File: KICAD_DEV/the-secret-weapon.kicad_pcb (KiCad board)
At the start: 6 copper layers, 150 x 150 mm, 44 parts, among them J1 USB_C_Receptacle_USB2.0_14P, J2 Screw_Terminal_01x02, SW1 SW_Push, SW2 SW_Push, U1 STM32H743VITx, U2 USBLC6-2SC6, U3 LMR33640ADDA, U4 LM1086S-3.3/TR, Y1 8 MHz, Y2 32.768 KHz

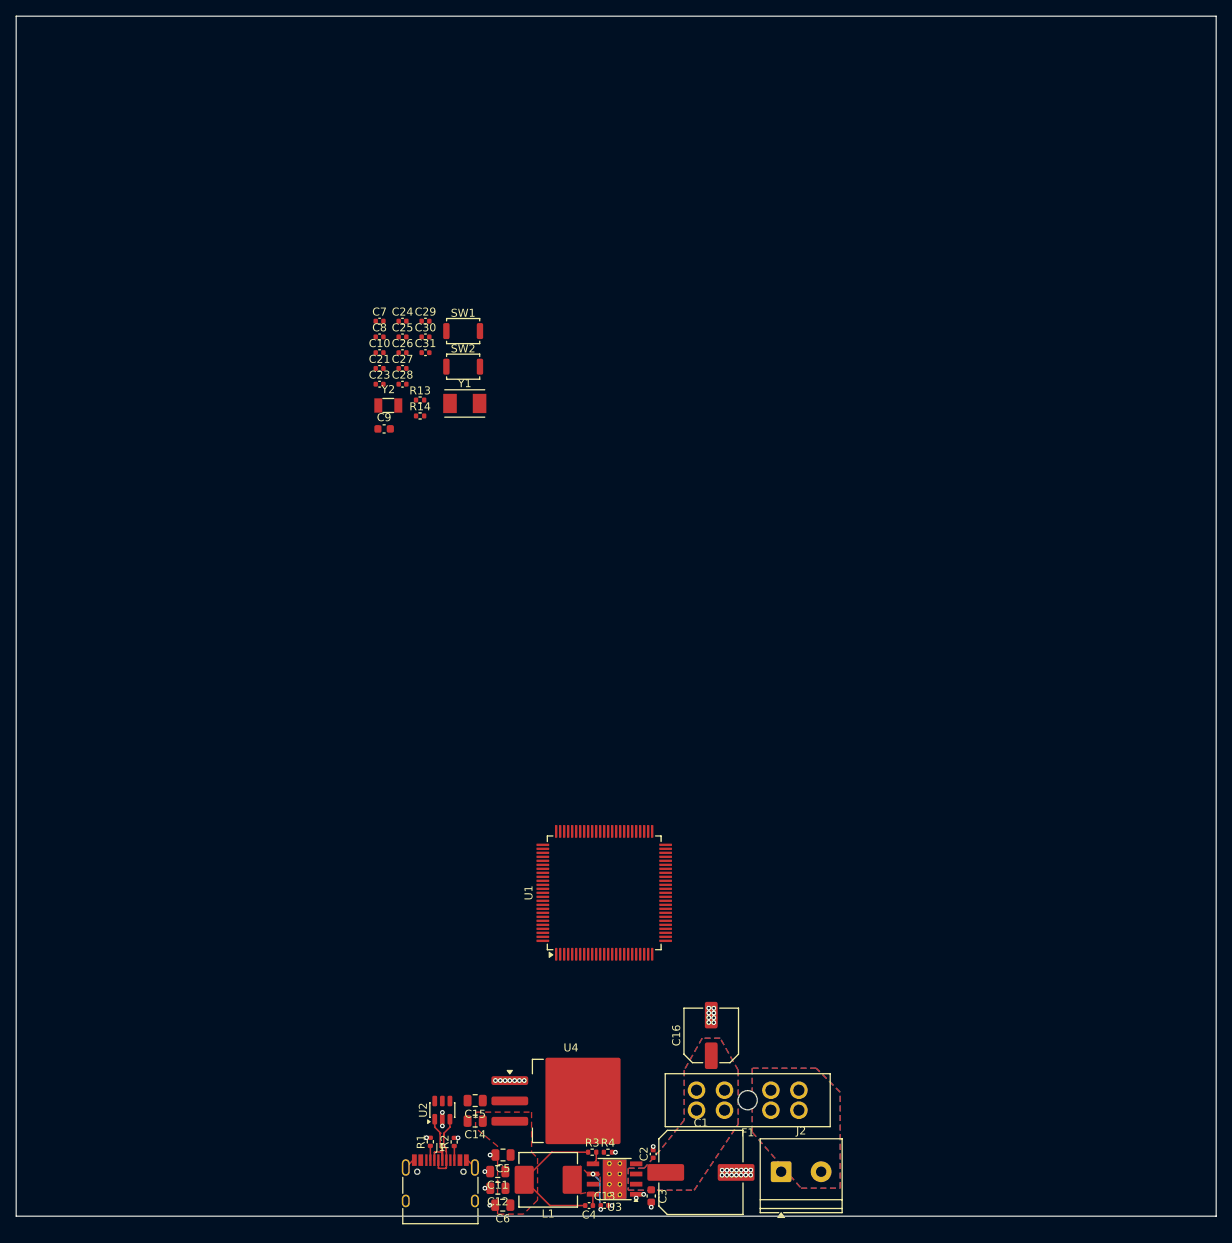
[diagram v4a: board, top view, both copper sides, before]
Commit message: finished routing the power!
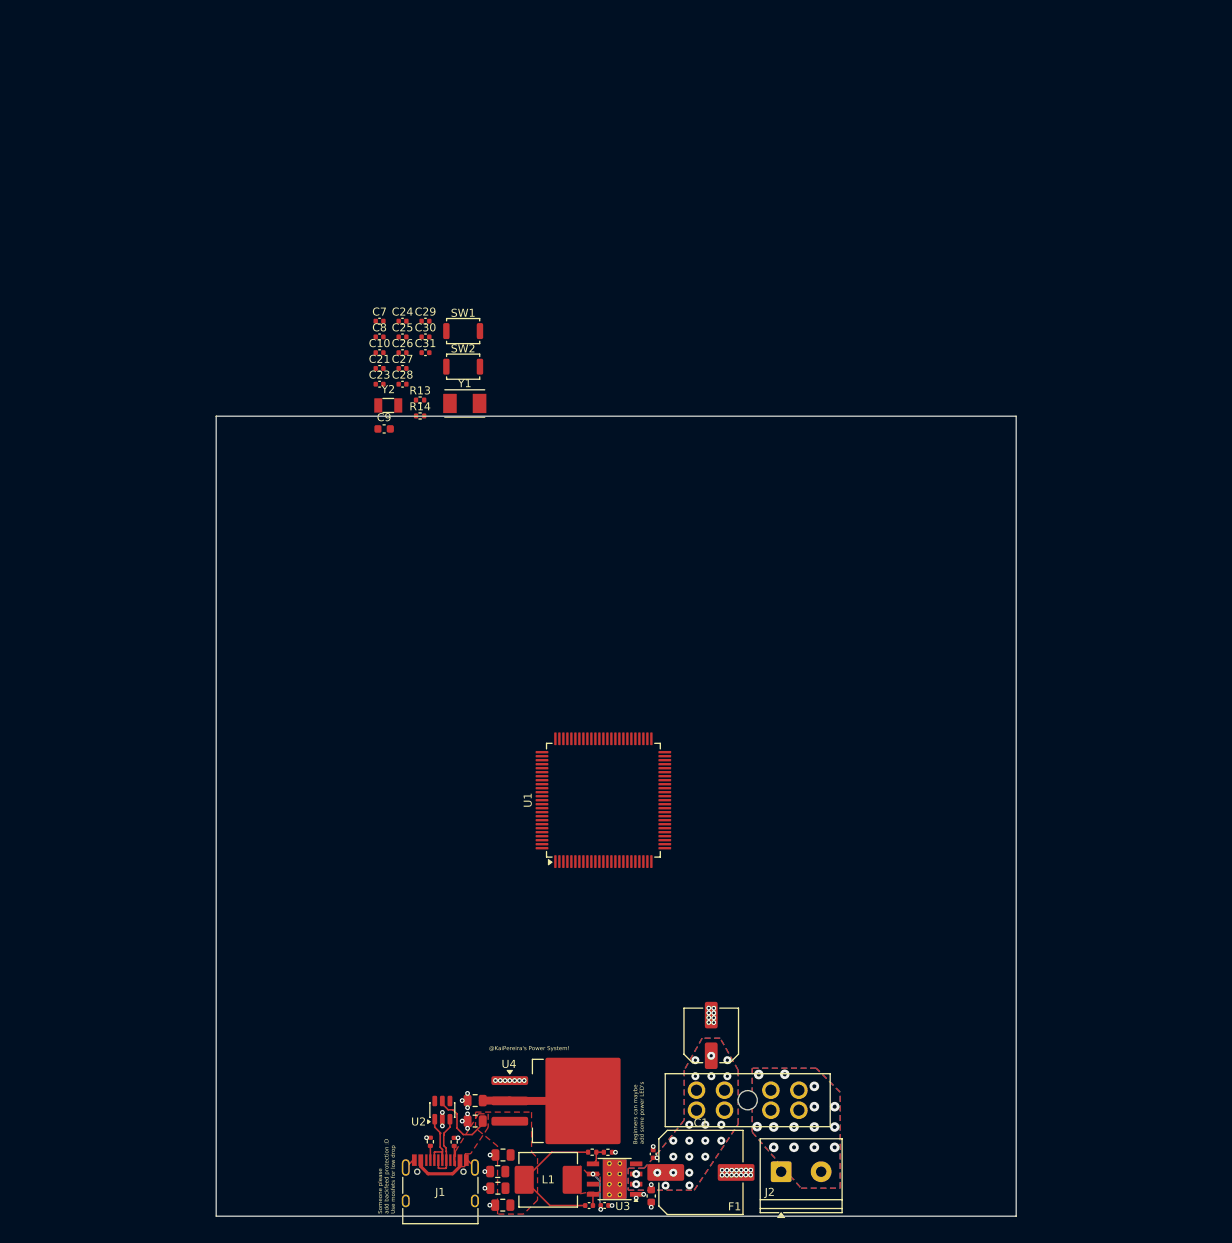
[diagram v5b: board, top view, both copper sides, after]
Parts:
- moved U1 11.6 mm to (144.4, 126.5)
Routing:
- net +5V: track 18.4 -> 34.6 mm
- net +3V3: track 0.00 -> 12.5 mm
- net GND: track 11.6 -> 16.5 mm, vias 43 -> 49
- net +12V: track 0.00 -> 1.12 mm, vias 0 -> 25
- net Net-(U3-FB): track 1.62 -> 2.58 mm
- net Net-(J2-Pin_2): vias 0 -> 14
- added copper zone on In2.Cu, net +12V
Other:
- board size 150 x 150 mm -> 100 x 100 mm
- board text added: "@KaiPereira's Power System!"
- board text added: "Beginners can maybe add some power LED's"
- board text added: "Someone please add backfeed protection :D Use mosfets for low drop"

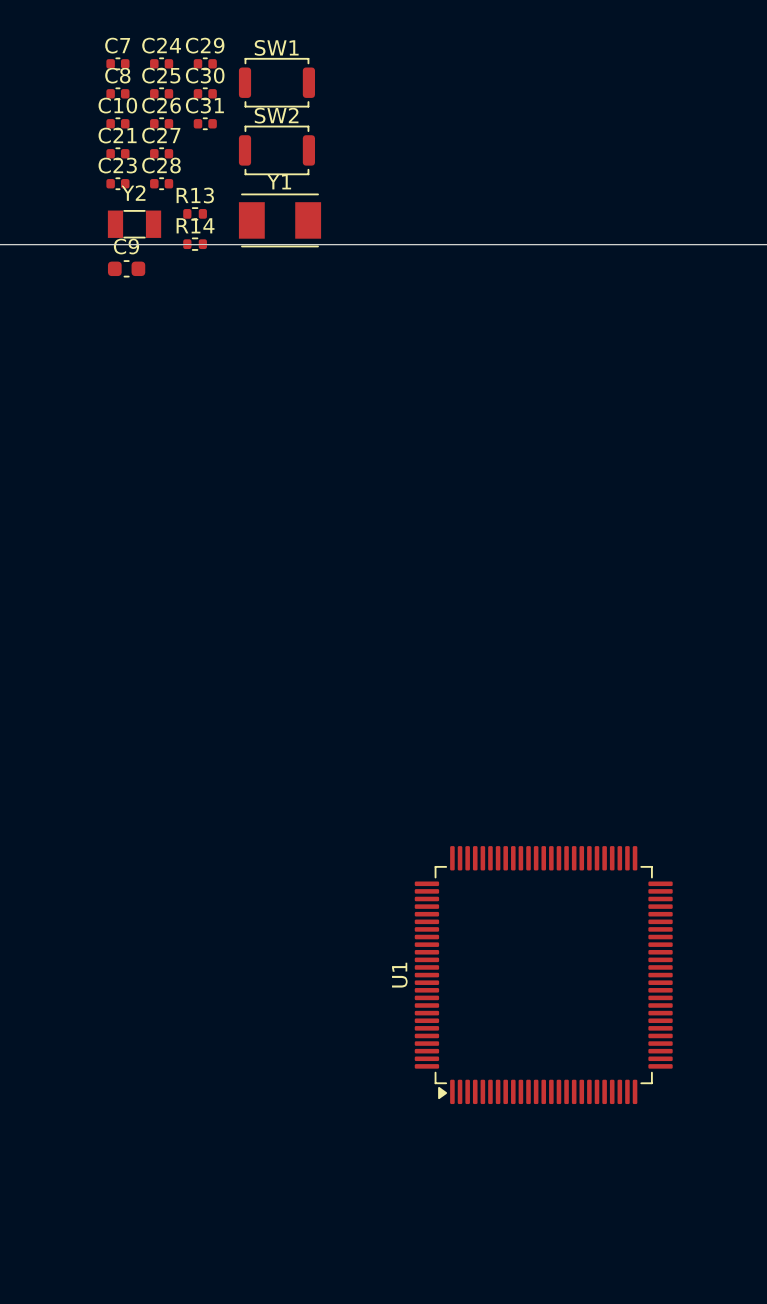
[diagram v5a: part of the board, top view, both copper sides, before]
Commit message: layed out the main SoC
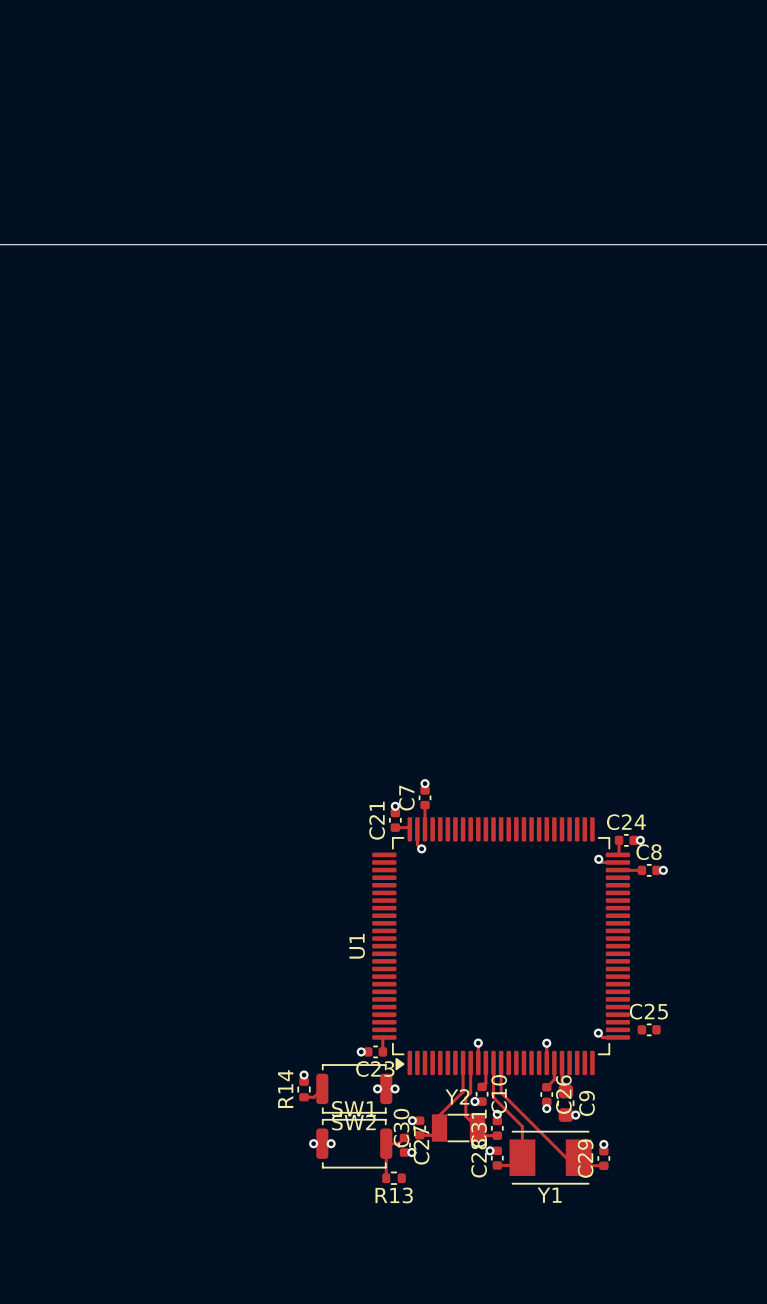
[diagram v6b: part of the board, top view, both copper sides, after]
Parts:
- moved C29 76.5 mm to (148.3, 138.6), turned to 90 degrees
- moved SW1 69.9 mm to (131.9, 137.6)
- moved C30 69.4 mm to (136.2, 136.6), turned to 90 degrees
- moved C25 69.4 mm to (151.3, 130.1)
- moved C31 68.7 mm to (141.3, 136.6), turned to 90 degrees
- moved C26 68.6 mm to (144.6, 134.3), turned to -90 degrees
- moved C10 68.1 mm to (140.3, 134.3), turned to -90 degrees
- moved C28 67.7 mm to (141.3, 138.5), turned to 90 degrees
- moved C27 67.1 mm to (135.2, 137.7), turned to -90 degrees
- moved R13 64.7 mm to (134.6, 139.8), turned to 180 degrees
- moved Y1 64.1 mm to (144.8, 138.5), turned to 180 degrees
- moved Y2 63.1 mm to (138.8, 136.6)
- moved C9 62.0 mm to (145.8, 134.9), turned to -90 degrees
- moved SW2 61.9 mm to (131.9, 134.0), turned to 180 degrees
- moved C8 61.8 mm to (151.3, 119.6)
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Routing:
- net GND: track 16.5 -> 31.0 mm, vias 49 -> 70
- net OSC_OUT: track 0.00 -> 10.7 mm
- net +3V3: track 12.5 -> 22.1 mm, vias 0 -> 2
- net OSC_IN: track 0.00 -> 8.87 mm
- net OSC32_IN: track 0.00 -> 6.42 mm
- net OSC32_OUT: track 0.00 -> 6.23 mm
- net RESET: track 0.00 -> 3.63 mm
- net Net-(C7-Pad1): track 0.00 -> 3.18 mm
- net BOOT: track 0.00 -> 1.43 mm
- added copper zone on In2.Cu, net +3V3

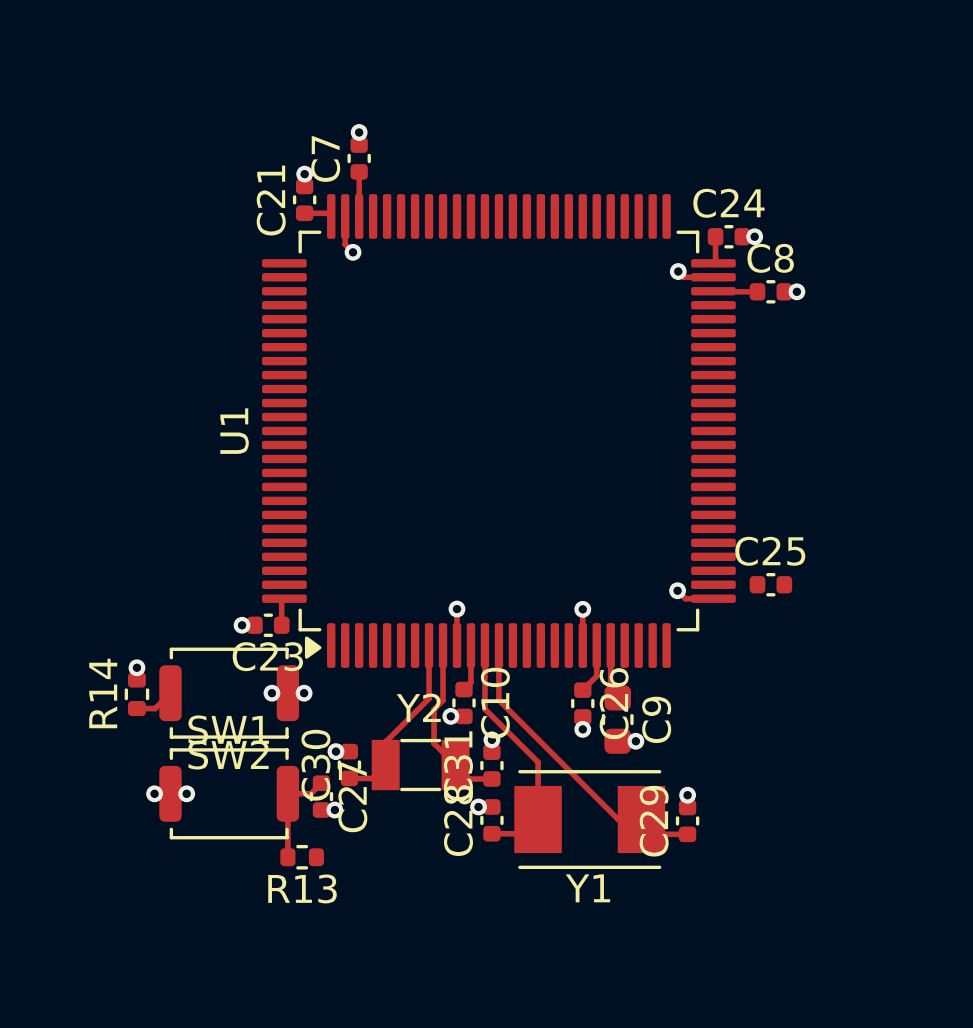
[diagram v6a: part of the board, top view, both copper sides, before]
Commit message: routed the SoC!
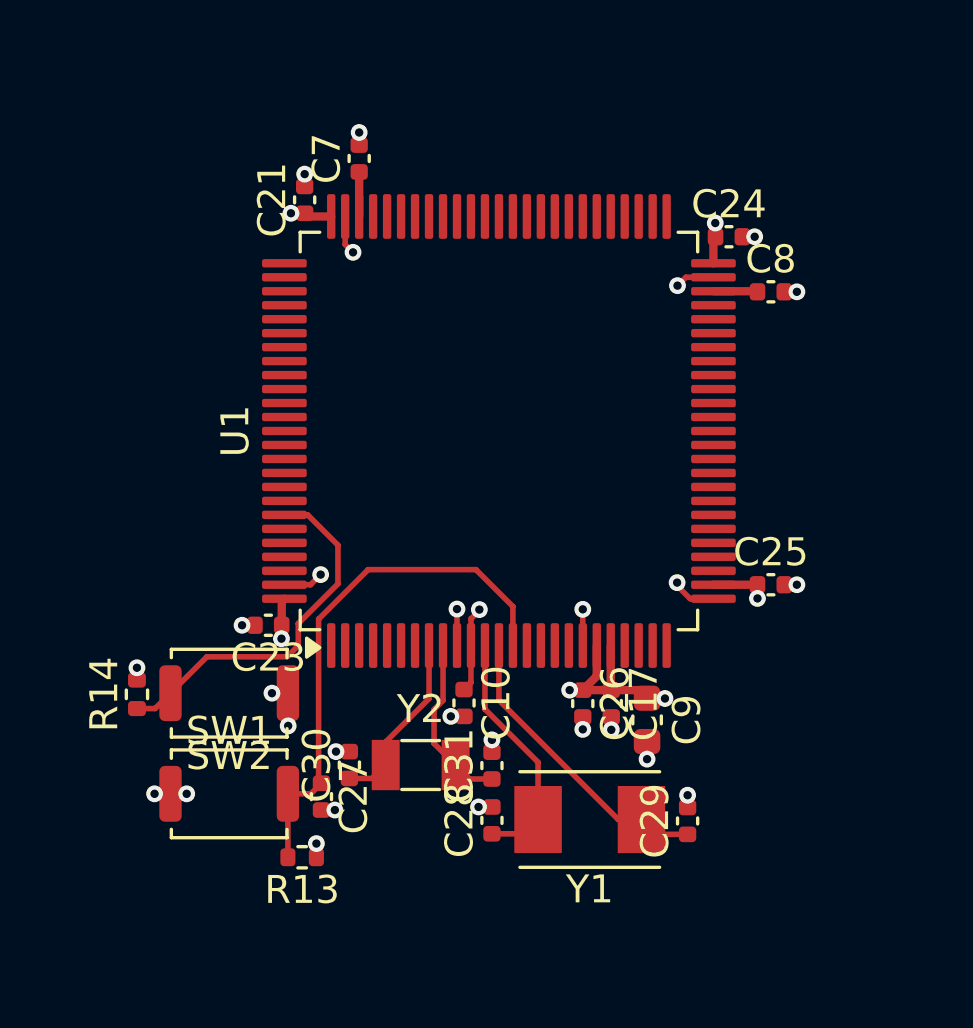
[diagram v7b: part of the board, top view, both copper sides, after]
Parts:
- added C17: 0.1uF, Capacitor_SMD:C_0402_1005Metric, F.Cu at (145.6, 134.3)
- moved C9 1.05 mm to (146.9, 134.9)
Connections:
- C8 pad 1: Net-(C7-Pad1) -> Net-(C8-Pad1)
- U1 pad 48: Net-(C7-Pad1) -> Net-(C8-Pad1)
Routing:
- net RESET: track 3.63 -> 19.2 mm
- net BOOT: track 1.43 -> 13.3 mm
- net +3V3: track 22.1 -> 31.3 mm, vias 2 -> 10
- net GND: track 31.0 -> 33.6 mm, vias 70 -> 73
- net Net-(C8-Pad1): track 0.00 -> 1.58 mm
- net Net-(C7-Pad1): track 3.18 -> 1.59 mm

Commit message: finished power routing, just have to add the power rails now!
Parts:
- moved C17 8.54 mm to (140.0, 140.8)
- moved C21 8.54 mm to (129.1, 122.8)
- moved C24 8.54 mm to (144.2, 124.1)
- moved C25 8.54 mm to (145.8, 136.6)
- moved C27 8.54 mm to (129.7, 144.2)
- moved C30 8.54 mm to (130.7, 143.0)
- moved C8 8.54 mm to (145.8, 126.1)
- moved C9 8.54 mm to (141.3, 141.4)
- moved R13 8.54 mm to (129.0, 146.3)
- moved R14 8.54 mm to (123.1, 140.5)
- moved Y2 8.54 mm to (133.2, 143.0)
- moved C23 8.54 mm to (127.8, 138.0)
- moved C10 8.54 mm to (134.8, 140.8)
- moved C26 8.54 mm to (139.0, 140.8)
- moved C28 8.54 mm to (135.8, 145.0)
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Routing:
- net +3V3: vias 10 -> 40
